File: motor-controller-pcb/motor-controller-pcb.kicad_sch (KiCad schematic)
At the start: 11 parts, among them J1 Conn_01x06_Pin, J2 Conn_01x06_Pin, J3 Conn_01x06_Pin, J4 Conn_01x06_Pin, J5 Conn_01x04_Pin, J6 Conn_01x04_Pin, M1 Conn_01x02_Pin, M2 Conn_01x02_Pin, M3 Conn_01x02_Pin, M4 Conn_01x02_Pin

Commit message: fix: change pcb footprint to jst ph
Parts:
- J1, J2, J3, J4: footprint Connector_JST:JST_SH_BM06B-SRSS-TB_1x06-1MP_P1.00mm_Vertical -> Connector_JST:JST_PH_B6B-PH-K_1x06_P2.00mm_Vertical
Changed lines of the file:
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@@
 			)
 		)
-		(property "Footprint" "Connector_JST:JST_SH_BM06B-SRSS-TB_1x06-1MP_P1.00mm_Vertical"
+		(property "Footprint" "Connector_JST:JST_PH_B6B-PH-K_1x06_P2.00mm_Vertical"
 			(at 80.01 138.43 0)
 			(effects
@@
 			)
 		)
-		(property "Footprint" "Connector_JST:JST_SH_BM06B-SRSS-TB_1x06-1MP_P1.00mm_Vertical"
+		(property "Footprint" "Connector_JST:JST_PH_B6B-PH-K_1x06_P2.00mm_Vertical"
 			(at 80.01 97.79 0)
 			(effects
@@
 			)
 		)
-		(property "Footprint" "Connector_JST:JST_SH_BM06B-SRSS-TB_1x06-1MP_P1.00mm_Vertical"
+		(property "Footprint" "Connector_JST:JST_PH_B6B-PH-K_1x06_P2.00mm_Vertical"
 			(at 80.01 77.47 0)
 			(effects
@@
 			)
 		)
-		(property "Footprint" "Connector_JST:JST_SH_BM06B-SRSS-TB_1x06-1MP_P1.00mm_Vertical"
+		(property "Footprint" "Connector_JST:JST_PH_B6B-PH-K_1x06_P2.00mm_Vertical"
 			(at 80.01 118.11 0)
 			(effects

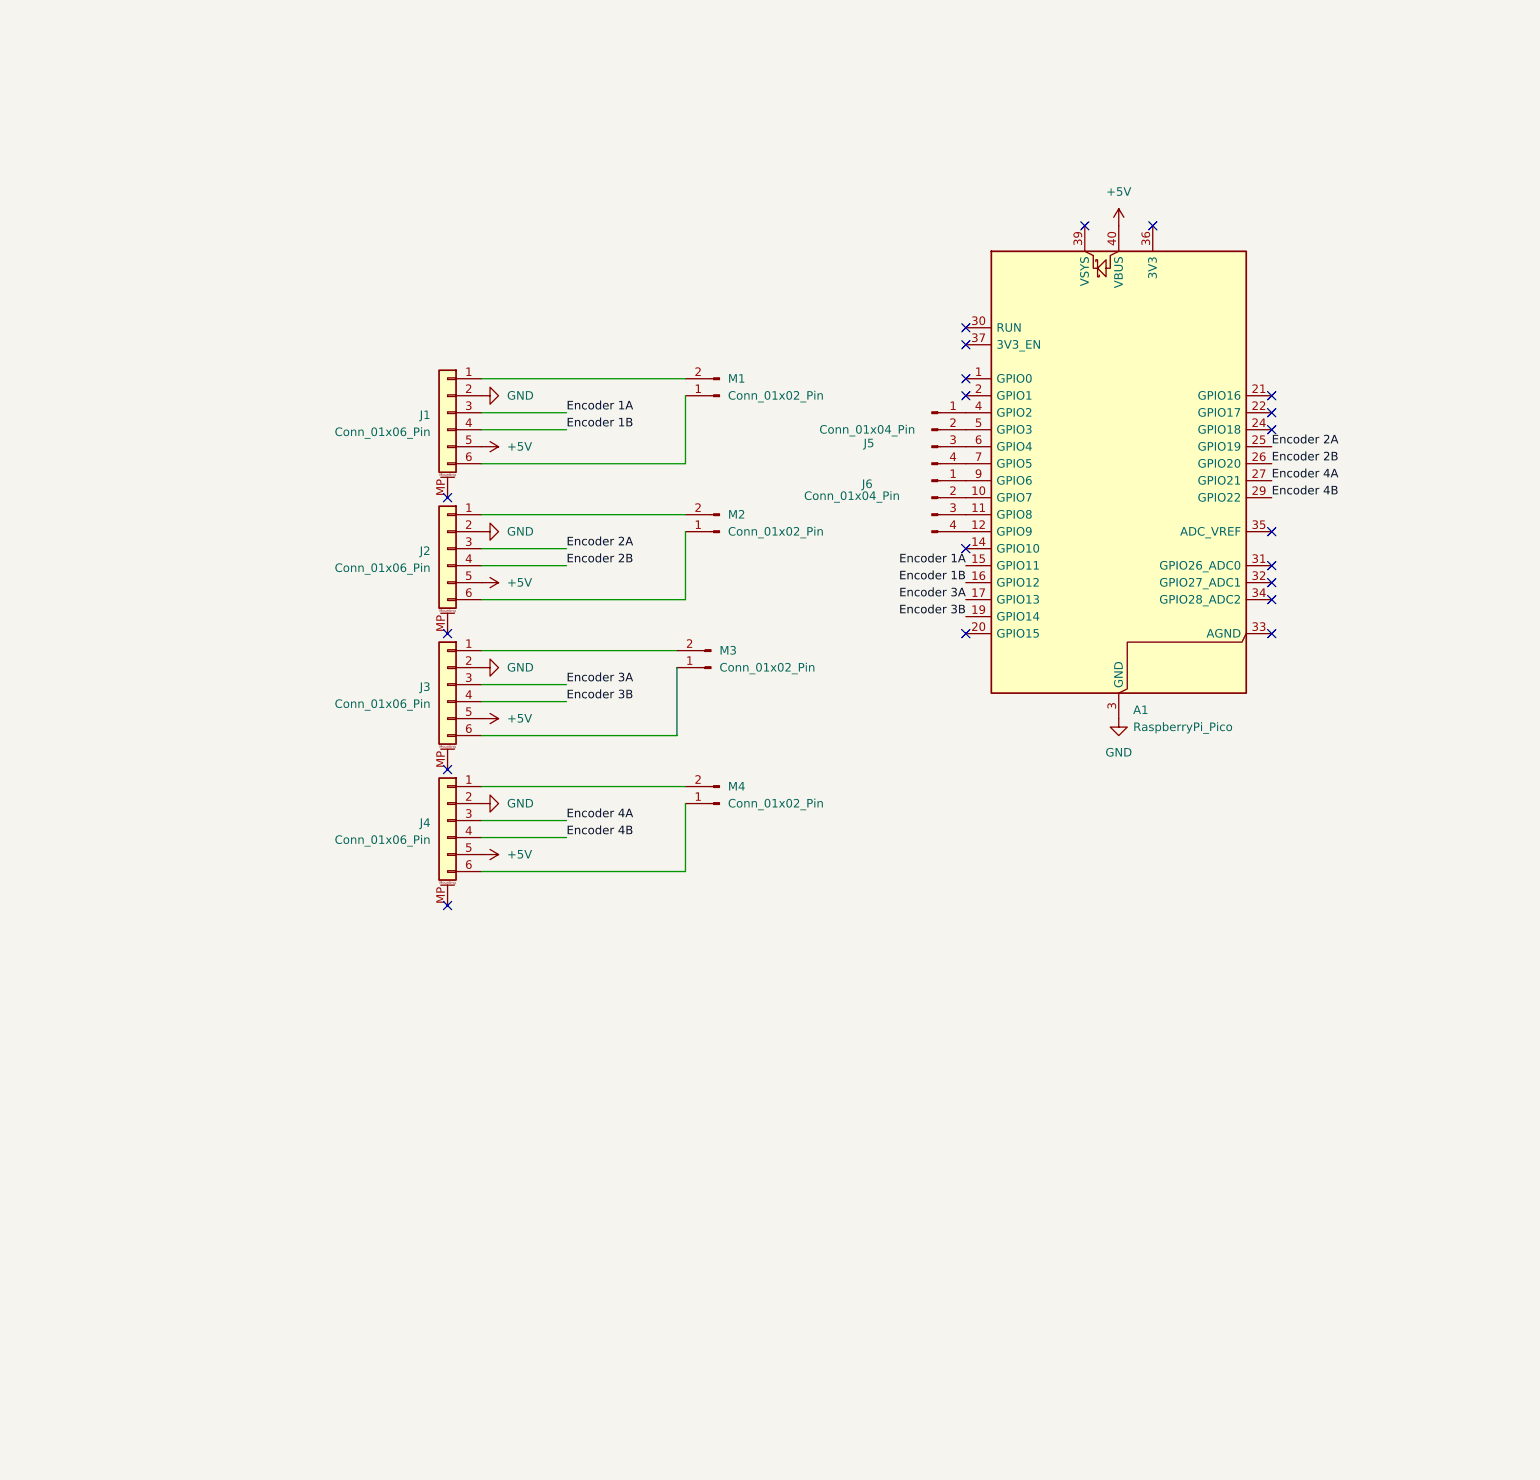
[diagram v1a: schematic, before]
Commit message: feat: schematic improvement
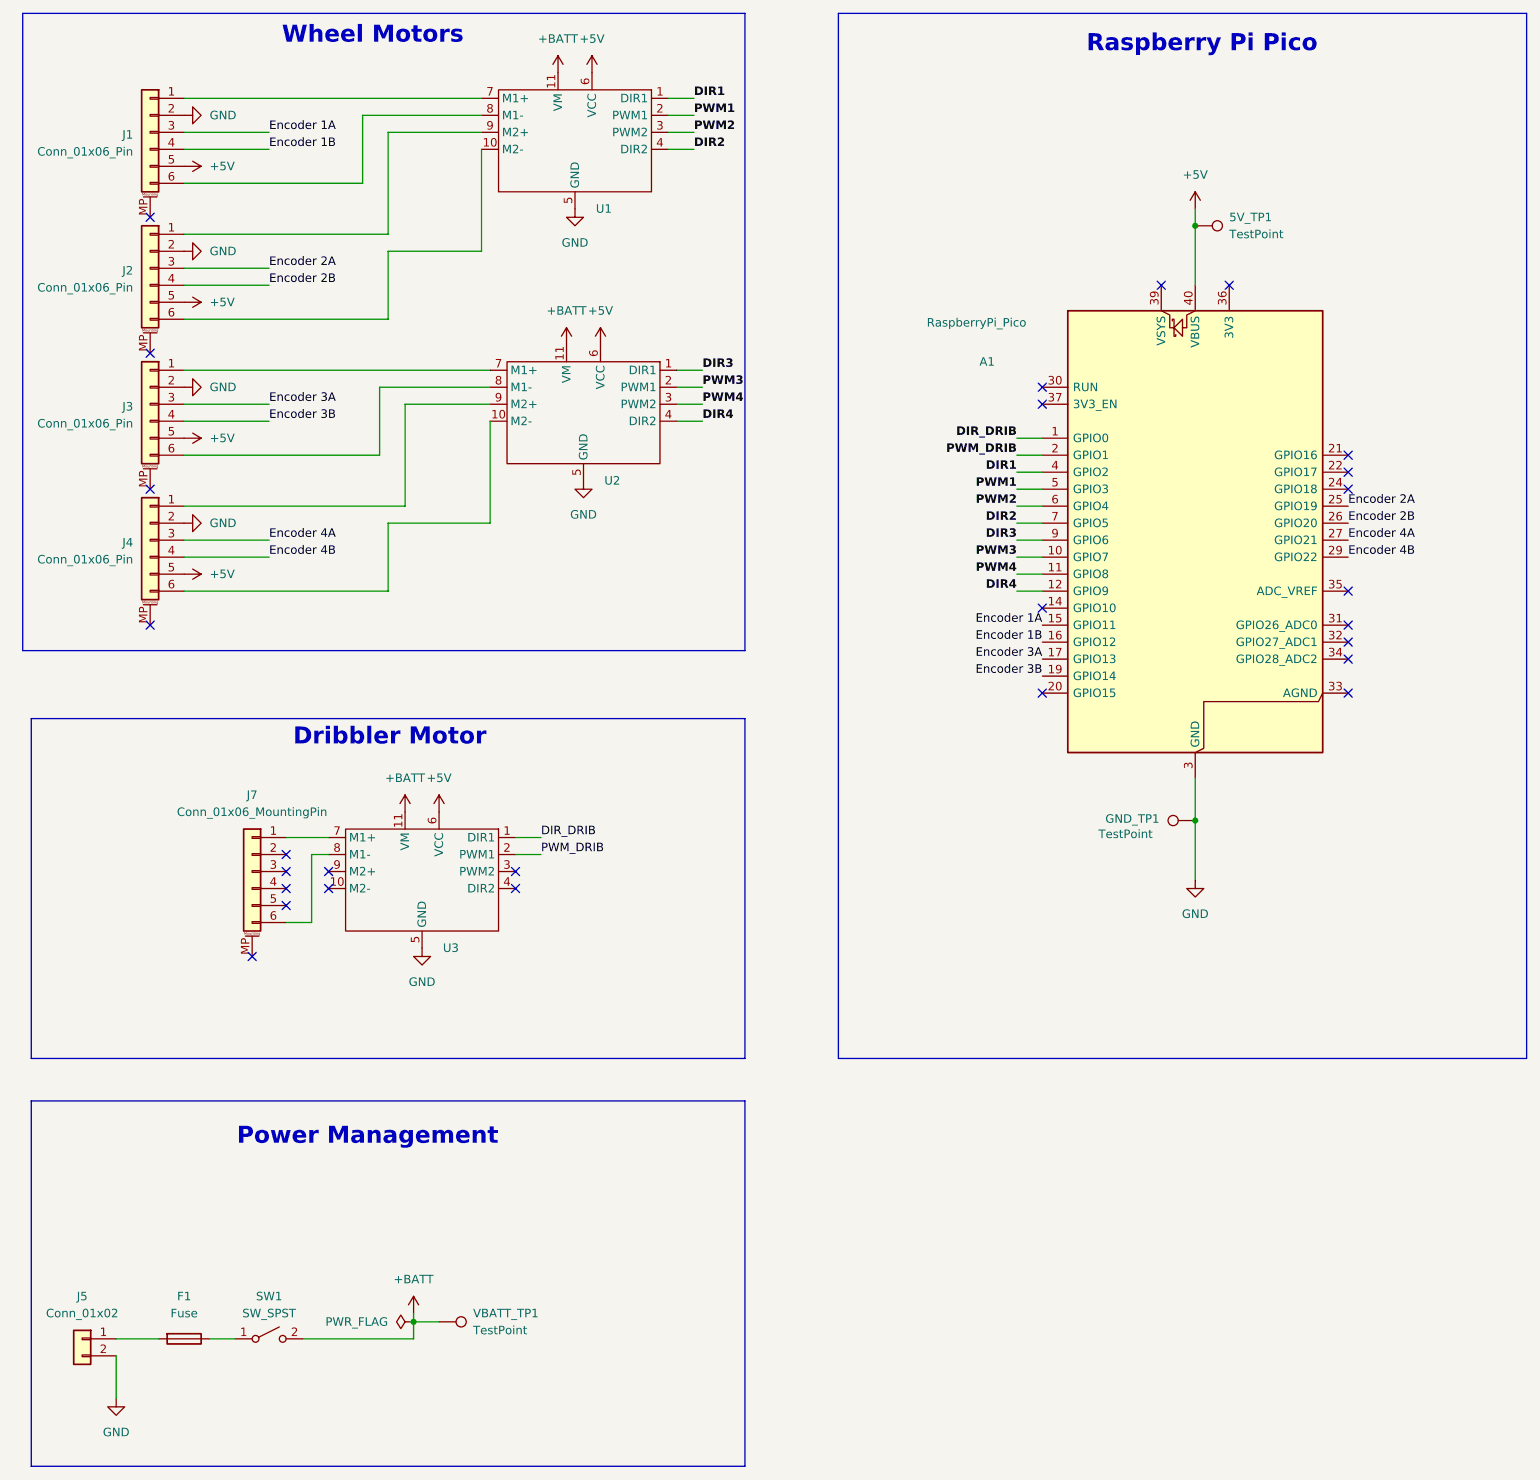
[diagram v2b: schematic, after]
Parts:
- removed J5, J6: Conn_01x04_Pin, Connector_PinHeader_2.54mm:PinHeader_1x04_P2.54mm_Vertical, symbol Connector:Conn_01x04_Pin
- removed M1, M2, M3, M4: Conn_01x02_Pin, Connector_PinHeader_2.54mm:PinHeader_1x02_P2.54mm_Vertical, symbol Connector:Conn_01x02_Pin
- added 5V_TP1, GND_TP1, VBATT_TP1: TestPoint, symbol Connector:TestPoint
- added F1: Fuse, Fuse:Fuseholder_Clip-5x20mm_Littelfuse_100_Inline_P20.50x4.60mm_D1.30mm_Horizontal, symbol Device:Fuse
- added J5: Conn_01x02, Connector_Wire:SolderWire-6sqmm_1x02_P14mm_D3.5mm_OD7mm_Relief2x, symbol Connector_Generic:Conn_01x02
- added J7: Conn_01x06_MountingPin, symbol Connector_Generic_MountingPin:Conn_01x06_MountingPin
- added SW1: SW_SPST, Connector_Wire:SolderWire-6sqmm_1x02_P14mm_D3.5mm_OD7mm_Relief2x, symbol Switch:SW_SPST
- added U1, U2, U3: ~, symbol robocup:DRI044
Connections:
- net +5V: now also 5V_TP1.1, U1.6 (VCC), U2.6 (VCC), U3.6 (VCC)
- net GND: now also GND_TP1.1, J5.2 (Pin_2), U1.5 (GND), U2.5 (GND), U3.5 (GND)
- net at J4.6 (Pin_6): now also U2.10 (M2-)
- net at J4.1 (Pin_1): now also U2.9 (M2+)
- net at J1.6 (Pin_6): now also U1.8 (M1-)
- net at J1.1 (Pin_1): now also U1.7 (M1+)
- net at J2.1 (Pin_1): now also U1.9 (M2+)
- net at J2.6 (Pin_6): now also U1.10 (M2-)
- net DIR_DRIB: now reaches A1.1 (GPIO0)
- net DIR_DRIB: now also U3.1 (DIR1)
- net PWM3: now reaches A1.10 (GPIO7)
- net PWM3: now also U2.2 (PWM1)
- net PWM4: now reaches A1.11 (GPIO8)
- net PWM4: now also U2.3 (PWM2)
- net DIR4: now reaches A1.12 (GPIO9)
- net DIR4: now also U2.4 (DIR2)
- net PWM_DRIB: now reaches A1.2 (GPIO1)
- net PWM_DRIB: now also U3.2 (PWM1)
- net DIR1: now reaches A1.4 (GPIO2)
- net DIR1: now also U1.1 (DIR1)
- net PWM1: now reaches A1.5 (GPIO3)
- net PWM1: now also U1.2 (PWM1)
- net PWM2: now reaches A1.6 (GPIO4)
- net PWM2: now also U1.3 (PWM2)
- net DIR2: now reaches A1.7 (GPIO5)
- net DIR2: now also U1.4 (DIR2)
- net DIR3: now reaches A1.9 (GPIO6)
- net DIR3: now also U2.1 (DIR1)
- net at J3.1 (Pin_1): now also U2.7 (M1+)
- net at J3.6 (Pin_6): now also U2.8 (M1-)
- new net: J7.1 (Pin_1), U3.7 (M1+)
- new net: J7.6 (Pin_6), U3.8 (M1-)
- new net: F1.1, SW1.1 (A)
- new net: F1.2, J5.1 (Pin_1)
- new net +BATT: SW1.2 (B), U1.11 (VM), U2.11 (VM), U3.11 (VM), VBATT_TP1.1
- no-connect marks 20 -> 27
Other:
- note added: "Dribbler Motor"
- note added: "Power Management"
- note added: "Raspberry Pi Pico"
- note added: "Wheel Motors"
- company: (none) -> Hamzah Ahmed
- title: (none) -> Motor controller PCB
- moved on the sheet: A1, J1, J2, J3, J4

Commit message: feat: capacitors and aux pins
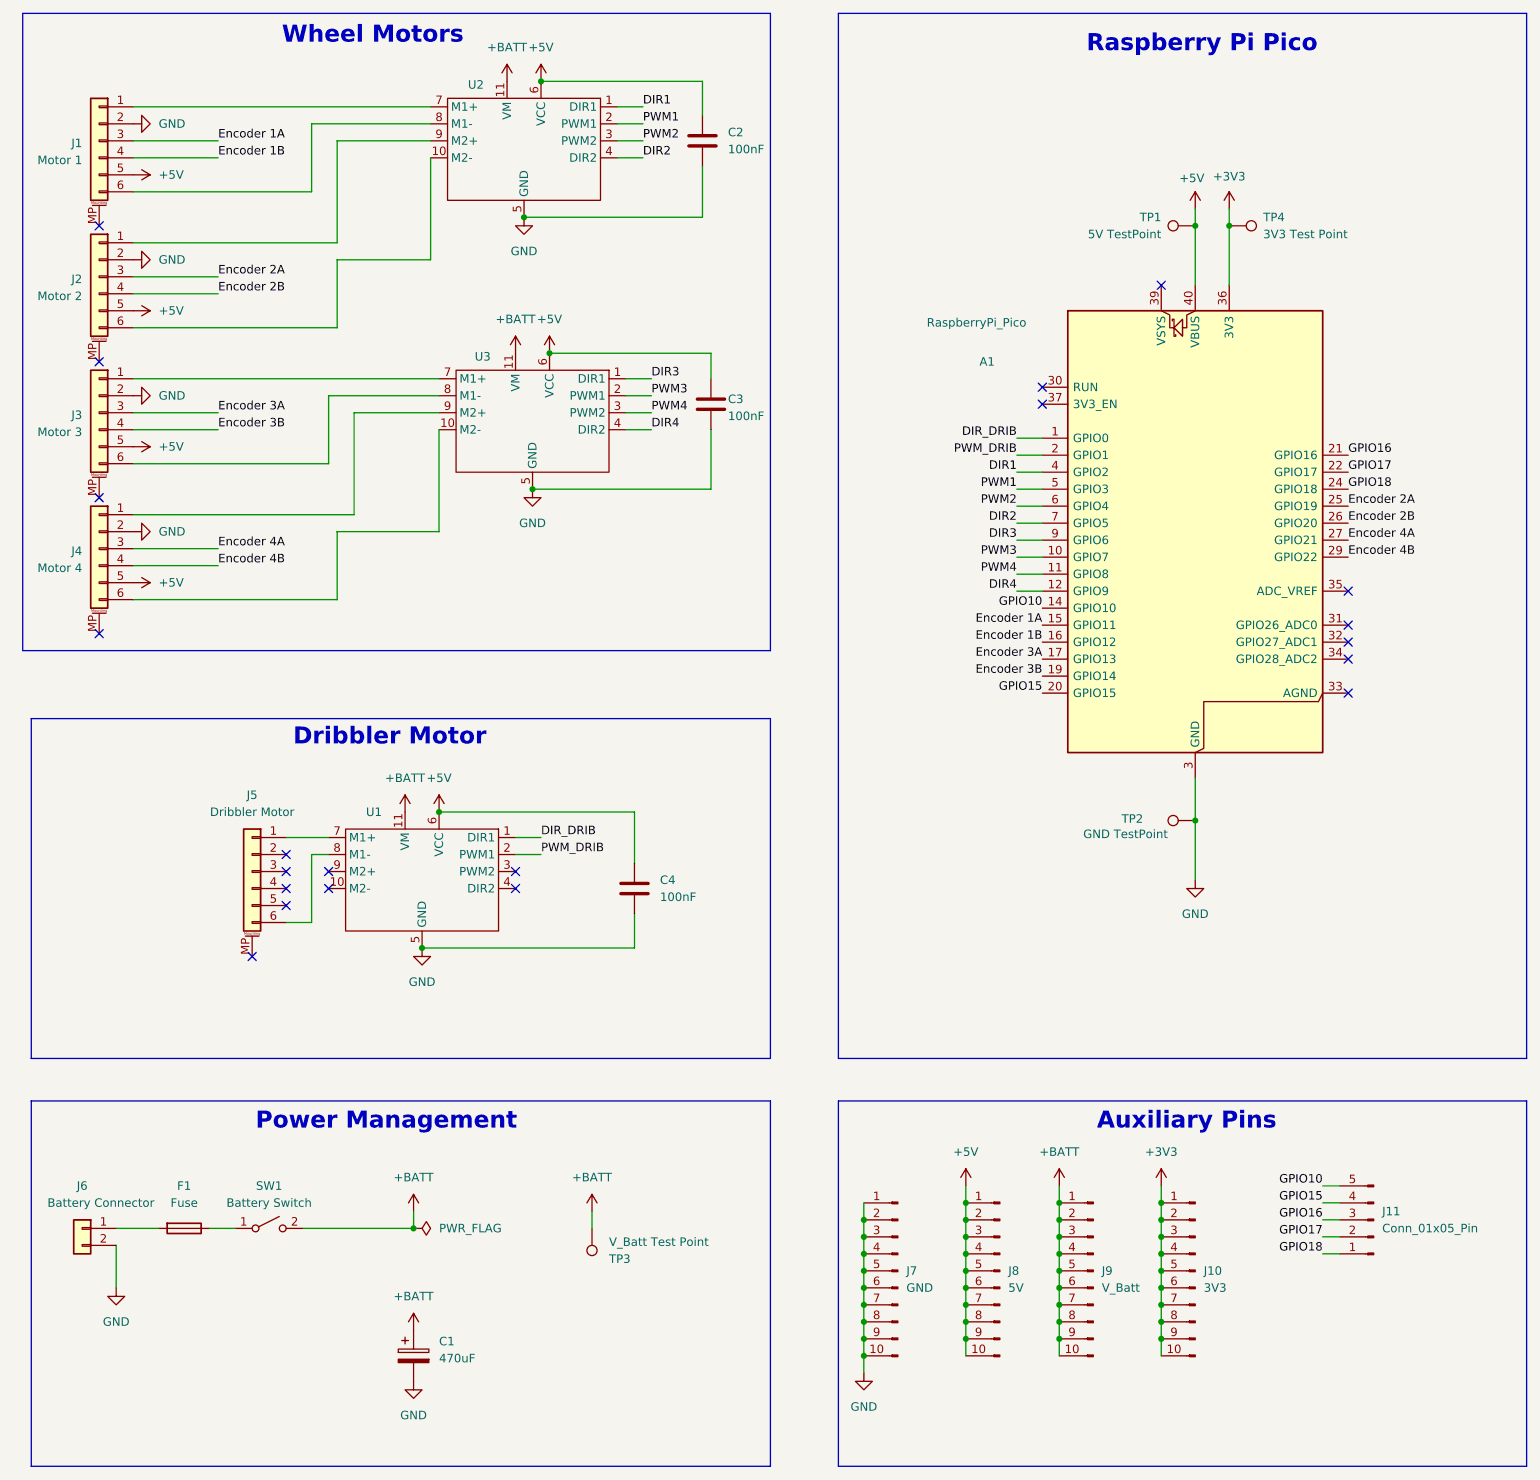
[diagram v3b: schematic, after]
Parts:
- added C1: 470uF, Capacitor_THT:CP_Radial_D8.0mm_P3.50mm, symbol Device:C_Polarized
- added C2, C3, C4: 100nF, Capacitor_SMD:C_0805_2012Metric, symbol Device:C
- added J10: 3V3, Connector_PinHeader_2.54mm:PinHeader_1x10_P2.54mm_Vertical, symbol Connector:Conn_01x10_Pin
- added J11: Conn_01x05_Pin, Connector_PinHeader_2.54mm:PinHeader_1x05_P2.54mm_Vertical, symbol Connector:Conn_01x05_Pin
- added J7: GND, Connector_PinHeader_2.54mm:PinHeader_1x10_P2.54mm_Vertical, symbol Connector:Conn_01x10_Pin
- added J8: 5V, Connector_PinHeader_2.54mm:PinHeader_1x10_P2.54mm_Vertical, symbol Connector:Conn_01x10_Pin
- added J9: V_Batt, Connector_PinHeader_2.54mm:PinHeader_1x10_P2.54mm_Vertical, symbol Connector:Conn_01x10_Pin
- added TP4: 3V3 Test Point, TestPoint:TestPoint_Pad_1.5x1.5mm, symbol Connector:TestPoint
- J1: value Conn_01x06_Pin -> Motor 1
- J2: value Conn_01x06_Pin -> Motor 2
- J3: value Conn_01x06_Pin -> Motor 3
- J4: value Conn_01x06_Pin -> Motor 4
- J5: renamed from J7; value Conn_01x06_MountingPin -> Dribbler Motor; footprint (none) -> Connector_JST:JST_PH_B6B-PH-K_1x06_P2.00mm_Vertical
- J6: renamed from J5; value Conn_01x02 -> Battery Connector
- SW1: value SW_SPST -> Battery Switch
- TP1: renamed from 5V_TP1; value TestPoint -> 5V TestPoint; footprint (none) -> TestPoint:TestPoint_Pad_1.5x1.5mm
- TP2: renamed from GND_TP1; value TestPoint -> GND TestPoint; footprint (none) -> TestPoint:TestPoint_Pad_1.5x1.5mm
- TP3: renamed from VBATT_TP1; value TestPoint -> V_Batt Test Point; footprint (none) -> TestPoint:TestPoint_Pad_1.5x1.5mm
- renumbered U3 to U1, U1 to U2, U2 to U3
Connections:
- net +5V: now also C2.1, C3.1, C4.1, J8.1 (Pin_1), J8.10 (Pin_10), J8.2 (Pin_2), J8.3 (Pin_3), J8.4 (Pin_4), J8.5 (Pin_5), J8.6 (Pin_6), J8.7 (Pin_7), J8.8 (Pin_8), J8.9 (Pin_9)
- net +BATT: now also C1.1, J9.1 (Pin_1), J9.10 (Pin_10), J9.2 (Pin_2), J9.3 (Pin_3), J9.4 (Pin_4), J9.5 (Pin_5), J9.6 (Pin_6), J9.7 (Pin_7), J9.8 (Pin_8), J9.9 (Pin_9)
- net GND: now also C1.2, C2.2, C3.2, C4.2, J7.1 (Pin_1), J7.10 (Pin_10), J7.2 (Pin_2), J7.3 (Pin_3), J7.4 (Pin_4), J7.5 (Pin_5), J7.6 (Pin_6), J7.7 (Pin_7), J7.8 (Pin_8), J7.9 (Pin_9)
- net GPIO10: now reaches A1.14 (GPIO10)
- net GPIO10: now also J11.5 (Pin_5)
- net GPIO15: now reaches A1.20 (GPIO15)
- net GPIO15: now also J11.4 (Pin_4)
- net GPIO16: now reaches A1.21 (GPIO16)
- net GPIO16: now also J11.3 (Pin_3)
- net GPIO17: now reaches A1.22 (GPIO17)
- net GPIO17: now also J11.2 (Pin_2)
- net GPIO18: now reaches A1.24 (GPIO18)
- net GPIO18: now also J11.1 (Pin_1)
- net +3V3: now reaches A1.36 (3V3)
- net +3V3: now also J10.1 (Pin_1), J10.10 (Pin_10), J10.2 (Pin_2), J10.3 (Pin_3), J10.4 (Pin_4), J10.5 (Pin_5), J10.6 (Pin_6), J10.7 (Pin_7), J10.8 (Pin_8), J10.9 (Pin_9), TP4.1
- no-connect marks 27 -> 21
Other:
- note added: "Auxiliary Pins"
- moved on the sheet: F1, J1, J2, J3, J4, J6, SW1, TP1, TP3, U2, U3
